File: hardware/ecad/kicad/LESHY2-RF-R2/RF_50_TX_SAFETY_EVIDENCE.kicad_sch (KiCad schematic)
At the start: 98 parts, among them J13 Samtec FTSH-105-01-L-DV-K-P-TR, Q6 Diodes Incorporated 2N7002DW-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, SW5 C&K JS102011SAQN, U107 Diodes Incorporated BAT54-7-F, U108 TLV1821DCKR, U109 TLV1821DCKR, U110 TLV1821DCKR, U111 TCA9535PWR, U112 BAT54ALT1G, U113 BAT54ALT1G, U114 BAT54ALT1G, U115 BAT54ALT1G, U116 BAT54ALT1G, U117 74LVC2G14GV,125, U118 SN74LVC3G07DCUR, U119 SN74LVC08APWR, U120 SN74LVC1G74DCUR, U121 74LVC1G32GV,125, U122 SN74LVC1G17DCKR, U123 Texas Instruments SN74LVC1G06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, U124 SN74LVC1G07DCKR, U125 TPS3808G33DBVR, U126 Texas Instruments TPD4E05U06D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, U127 Texas Instruments MSPM0C1106S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, U128 SN74LVC1G07DCKR, U129 SN74LVC1G07DCKR, U130 Texas Instruments TPS3435CAKA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, U131 SN74LVC1G07DCKR, U132 SN74LVC1G07DCKR, U133 Diodes Incorporated BAT54-7-F, U134 Diodes Incorporated BAT54-7-F

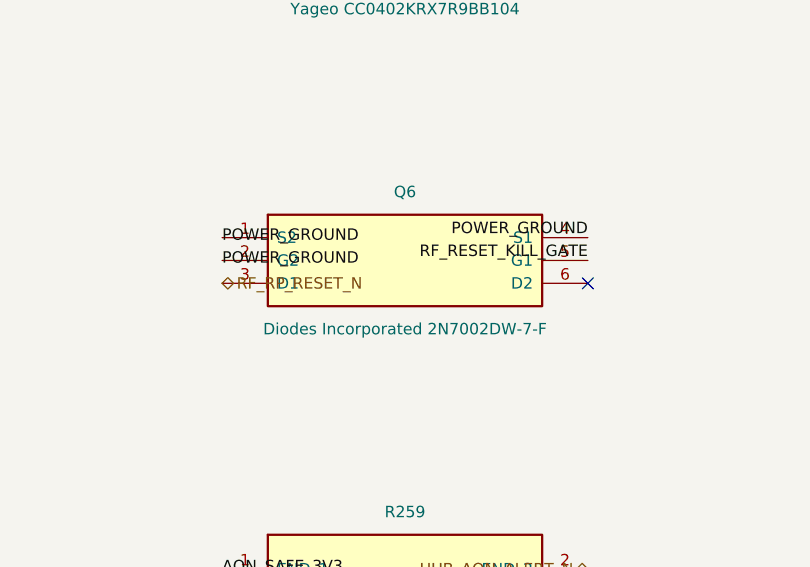
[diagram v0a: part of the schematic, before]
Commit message: Repair C5 service mux controls without weakening hardware KILL
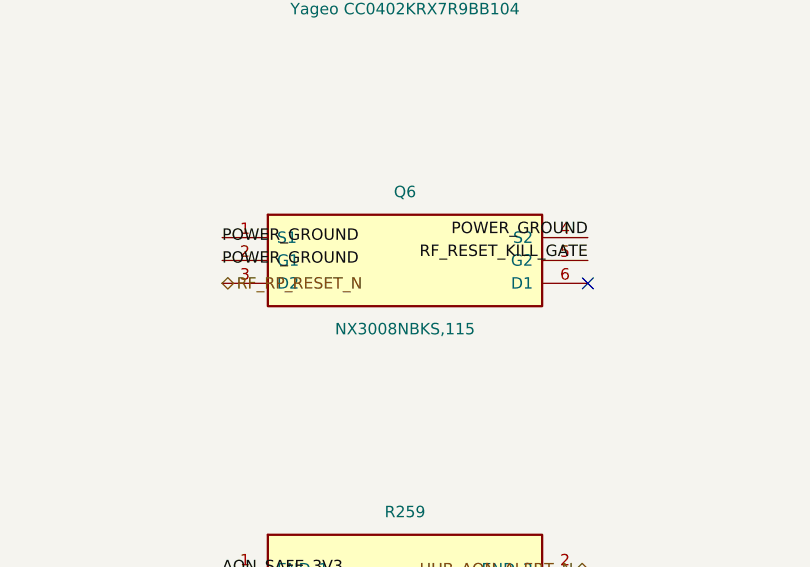
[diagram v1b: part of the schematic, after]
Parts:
- Q6: value Diodes Incorporated 2N7002DW-7-F -> NX3008NBKS,115; symbol Leshy2_R2:diodes_2n7002dw_7_f -> Leshy2_R2:nexperia_nx3008nbks_115
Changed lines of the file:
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@@
 	)
 	(symbol
-		(lib_id "Leshy2_R2:diodes_2n7002dw_7_f")
+		(lib_id "Leshy2_R2:nexperia_nx3008nbks_115")
 		(at 421.64 123.19 0)
 		(unit 1)
@@
 			(effects (font (size 1.27 1.27)))
 		)
-		(property "Value" "Diodes Incorporated 2N7002DW-7-F"
+		(property "Value" "NX3008NBKS,115"
 			(at 421.64 130.81 0)
 			(show_name no)
@@
 			(effects (font (size 1.27 1.27)))
 		)
-		(property "Description" "diodes_2n7002dw_7_f"
+		(property "Description" "nexperia_nx3008nbks_115"
 			(at 421.64 123.19 0)
 			(show_name no)
